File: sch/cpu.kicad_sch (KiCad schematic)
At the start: 10 parts

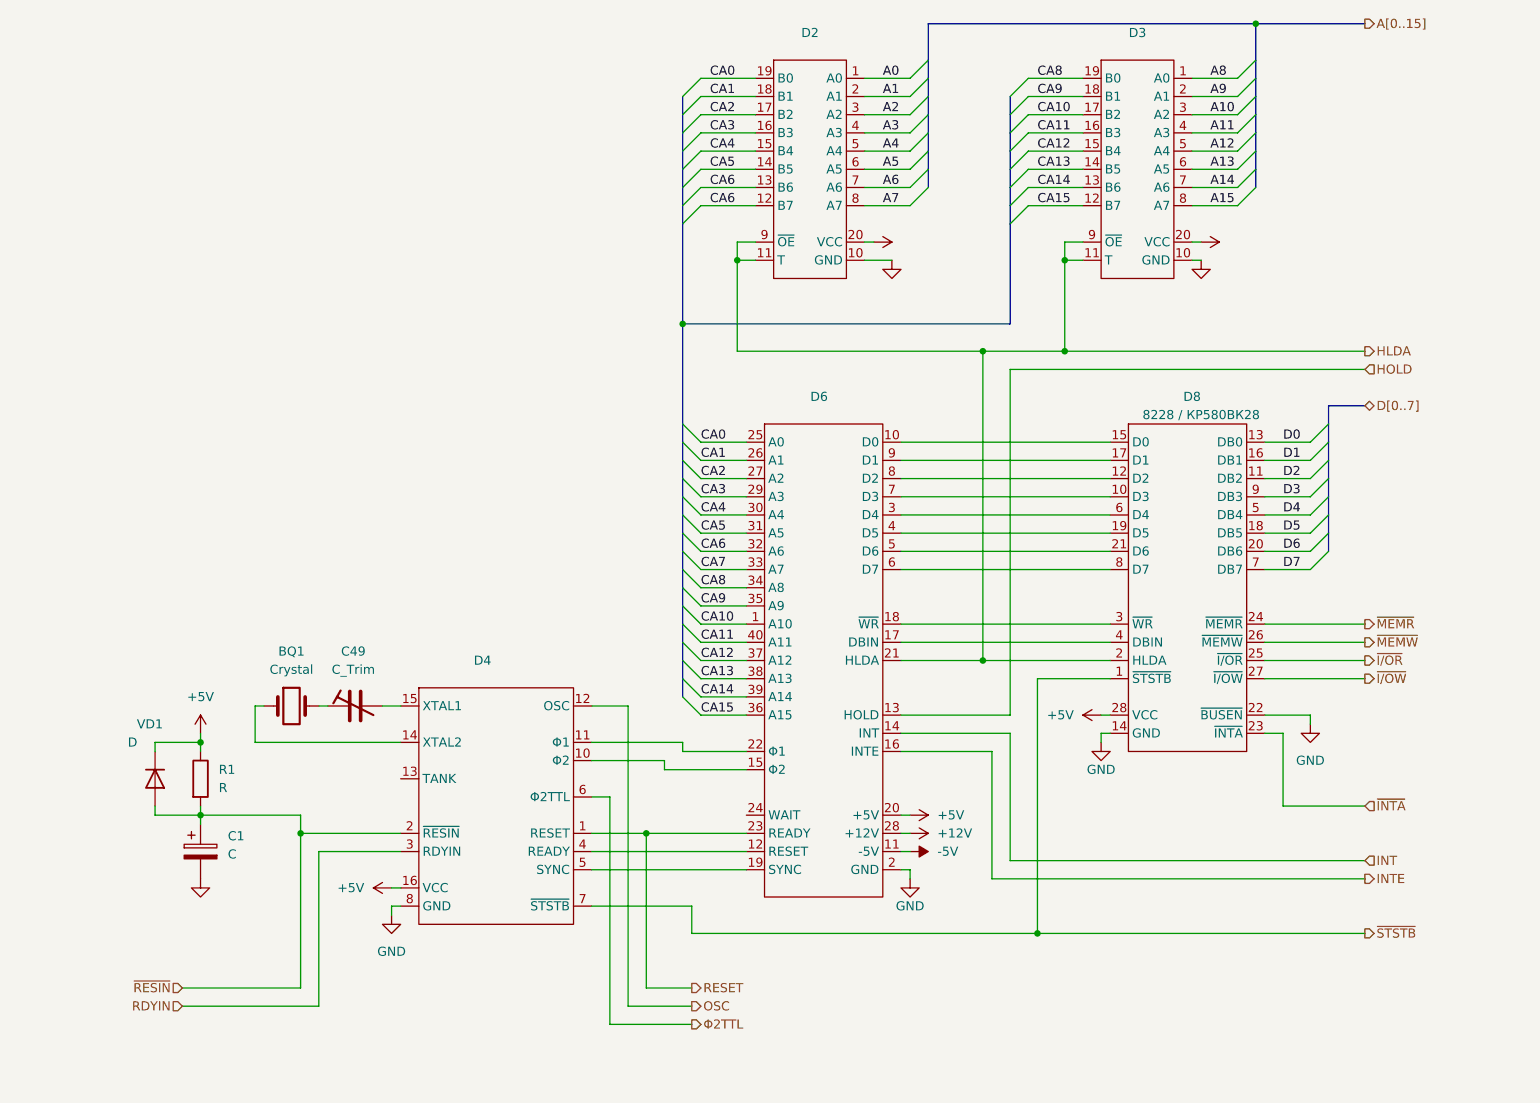
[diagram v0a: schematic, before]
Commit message: Schematic: ROM block
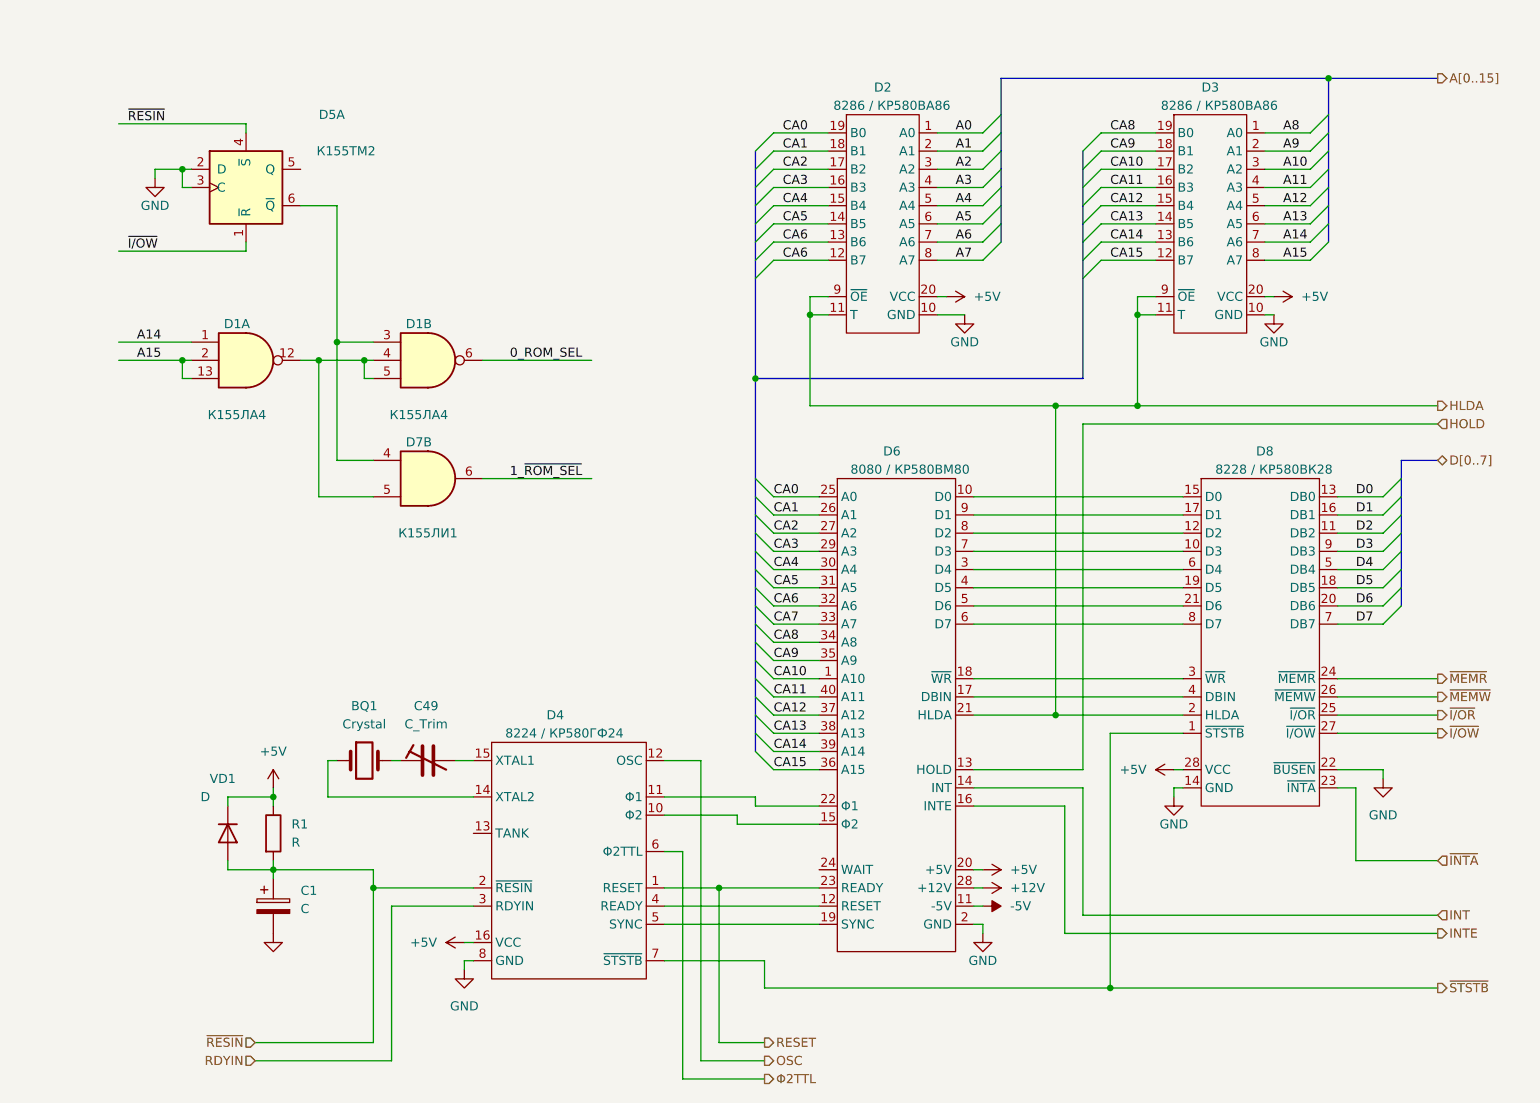
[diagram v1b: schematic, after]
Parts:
- added D1: (no value), symbol 74xx:74LS10
- added D5: (no value), symbol 74xx:74LS74
- added D7: (no value), symbol 74xx:74LS08
- D2, D3: value (none) -> 8286 / КР580ВА86
- D4: value (none) -> 8224 / КР580ГФ24
- D6: value (none) -> 8080 / КР580ВМ80
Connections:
- net A14: now also D1.1
- net A15: now also D1.13, D1.2
- net GND: now also D5.2 (D), D5.3 (C)
- net ~{I/OW}: now also D5.1 (~{R})
- net ~{RESIN}: now also D5.4 (~{S})
- new net: D1.3, D5.6 (~{Q}), D7.4
- new net: D1.12, D1.4, D1.5, D7.5
- new net 0_ROM_SEL: D1.6
- new net 1_~{ROM_SEL}: D7.6
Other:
- moved on the sheet: BQ1, C1, C49, D2, D3, D4, D6, D8, R1, VD1

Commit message: Added RAM block schematic placeholder
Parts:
- D1: value (none) -> 7410
- D5: value (none) -> 74LS74
- D7: value (none) -> 7408
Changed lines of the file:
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@@
     (in_bom yes) (on_board yes)
     (property "Reference" "D1" (id 0) (at 76.2 60.96 0))
-    (property "Value" "" (id 1) (at 76.2 71.12 0))
+    (property "Value" "7410" (id 1) (at 76.2 71.12 0))
     (property "Footprint" "" (id 2) (at 77.47 66.04 0)
       (effects (font (size 1.27 1.27)) hide)
@@
     (in_bom yes) (on_board yes)
     (property "Reference" "D1" (id 0) (at 50.8 60.96 0))
-    (property "Value" "" (id 1) (at 50.8 71.12 0))
+    (property "Value" "7410" (id 1) (at 50.8 71.12 0))
     (property "Footprint" "" (id 2) (at 52.07 66.04 0)
       (effects (font (size 1.27 1.27)) hide)
@@
       (effects (font (size 1.27 1.27)) (justify left))
     )
-    (property "Value" "" (id 1) (at 62.23 34.29 0)
+    (property "Value" "74LS74" (id 1) (at 62.23 34.29 0)
       (effects (font (size 1.27 1.27)) (justify left))
     )
@@
     (in_bom yes) (on_board yes)
     (property "Reference" "D7" (id 0) (at 76.2 77.47 0))
-    (property "Value" "" (id 1) (at 76.2 87.63 0))
+    (property "Value" "7408" (id 1) (at 76.2 87.63 0))
     (property "Footprint" "" (id 2) (at 77.47 82.55 0)
       (effects (font (size 1.27 1.27)) hide)

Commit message: Sch: CPU sheet - corrected address buffer pin assignment
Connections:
- net A10: now also D3.8 (A7); no longer D3.3 (A2)
- net A11: now also D3.7 (A6); no longer D3.4 (A3)
- net A12: now also D3.4 (A3); no longer D3.5 (A4)
- net A13: now also D3.5 (A4); no longer D3.6 (A5)
- net A14: now also D3.6 (A5); no longer D3.7 (A6)
- net A15: now also D3.3 (A2); no longer D3.8 (A7)
- net CA10: now also D3.12 (B7); no longer D3.17 (B2)
- net CA11: now also D3.13 (B6); no longer D3.16 (B3)
- net CA12: now also D3.16 (B3); no longer D3.15 (B4)
- net CA13: now also D3.15 (B4); no longer D3.14 (B5)
- net CA14: now also D3.14 (B5); no longer D3.13 (B6)
- net CA15: now also D3.17 (B2); no longer D3.12 (B7)
- net CA6: no longer D2.12 (B7)
- net CA7: now also D2.12 (B7)
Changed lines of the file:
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@@
     (stroke (width 0) (type default) (color 0 0 0 0))
   )
-  (label "A13" (at 196.85 46.99 0)
+  (label "A14" (at 196.85 46.99 0)
     (effects (font (size 1.27 1.27)) (justify left bottom))
   )
@@
     (effects (font (size 1.27 1.27)) (justify left bottom))
   )
-  (label "CA15" (at 172.72 52.07 0)
+  (label "CA10" (at 172.72 52.07 0)
     (effects (font (size 1.27 1.27)) (justify left bottom))
   )
@@
     (effects (font (size 1.27 1.27)) (justify left bottom))
   )
-  (label "CA11" (at 172.72 41.91 0)
+  (label "CA12" (at 172.72 41.91 0)
     (effects (font (size 1.27 1.27)) (justify left bottom))
   )
@@
     (effects (font (size 1.27 1.27)) (justify left bottom))
   )
-  (label "CA12" (at 172.72 44.45 0)
+  (label "CA13" (at 172.72 44.45 0)
     (effects (font (size 1.27 1.27)) (justify left bottom))
   )
-  (label "CA6" (at 127 52.07 0)
+  (label "CA7" (at 127 52.07 0)
     (effects (font (size 1.27 1.27)) (justify left bottom))
   )
@@
     (effects (font (size 1.27 1.27)) (justify left bottom))
   )
-  (label "CA13" (at 172.72 46.99 0)
+  (label "CA14" (at 172.72 46.99 0)
     (effects (font (size 1.27 1.27)) (justify left bottom))
   )
@@
     (effects (font (size 1.27 1.27)) (justify left bottom))
   )
-  (label "A12" (at 196.85 44.45 0)
+  (label "A13" (at 196.85 44.45 0)
     (effects (font (size 1.27 1.27)) (justify left bottom))
   )
@@
     (effects (font (size 1.27 1.27)) (justify left bottom))
   )
-  (label "CA10" (at 172.72 39.37 0)
+  (label "CA15" (at 172.72 39.37 0)
     (effects (font (size 1.27 1.27)) (justify left bottom))
   )
-  (label "A15" (at 196.85 52.07 0)
+  (label "A10" (at 196.85 52.07 0)
     (effects (font (size 1.27 1.27)) (justify left bottom))
   )
@@
     (effects (font (size 1.27 1.27)) (justify left bottom))
   )
-  (label "A11" (at 196.85 41.91 0)
+  (label "A12" (at 196.85 41.91 0)
     (effects (font (size 1.27 1.27)) (justify left bottom))
   )
@@
     (effects (font (size 1.27 1.27)) (justify left bottom))
   )
-  (label "CA14" (at 172.72 49.53 0)
+  (label "CA11" (at 172.72 49.53 0)
     (effects (font (size 1.27 1.27)) (justify left bottom))
   )
@@
     (effects (font (size 1.27 1.27)) (justify left bottom))
   )
-  (label "A10" (at 196.85 39.37 0)
+  (label "A15" (at 196.85 39.37 0)
     (effects (font (size 1.27 1.27)) (justify left bottom))
   )
@@
     (effects (font (size 1.27 1.27)) (justify left bottom))
   )
-  (label "A14" (at 196.85 49.53 0)
+  (label "A11" (at 196.85 49.53 0)
     (effects (font (size 1.27 1.27)) (justify left bottom))
   )

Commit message: Minor renames
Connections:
- net ~{REMAP}: now reaches D1.3, D5.6 (~{Q}), D7.4
- net 0_ROM_SEL renamed ROM_OE
- net 1_~{ROM_SEL} renamed ~{ROM_OE}
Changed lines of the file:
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@@
   (junction (at 118.11 139.7) (diameter 0) (color 0 0 0 0)
   )
-  (junction (at 64.77 63.5) (diameter 0) (color 0 0 0 0)
-  )
   (junction (at 123.19 68.58) (diameter 0) (color 0 0 0 0)
   )
   (junction (at 62.23 66.04) (diameter 0) (color 0 0 0 0)
   )
+  (junction (at 68.58 63.5) (diameter 0) (color 0 0 0 0)
+  )
   (junction (at 203.2 26.67) (diameter 0) (color 0 0 0 0)
   )
@@
     (stroke (width 0) (type default) (color 0 0 0 0))
   )
+  (wire (pts (xy 68.58 63.5) (xy 69.85 63.5))
+    (stroke (width 0) (type default) (color 0 0 0 0))
+  )
   (bus (pts (xy 123.19 113.03) (xy 123.19 115.57))
     (stroke (width 0) (type default) (color 0 0 0 0))
@@
     (stroke (width 0) (type default) (color 0 0 0 0))
   )
+  (wire (pts (xy 68.58 63.5) (xy 64.77 63.5))
+    (stroke (width 0) (type default) (color 0 0 0 0))
+  )
   (wire (pts (xy 110.49 142.24) (xy 132.08 142.24))
     (stroke (width 0) (type default) (color 0 0 0 0))
@@
     (stroke (width 0) (type default) (color 0 0 0 0))
   )
-  (wire (pts (xy 64.77 63.5) (xy 69.85 63.5))
-    (stroke (width 0) (type default) (color 0 0 0 0))
-  )
   (wire (pts (xy 153.67 139.7) (xy 154.94 139.7))
     (stroke (width 0) (type default) (color 0 0 0 0))
@@
     (stroke (width 0) (type default) (color 0 0 0 0))
   )
-  (wire (pts (xy 59.69 44.45) (xy 64.77 44.45))
+  (wire (pts (xy 59.69 44.45) (xy 68.58 44.45))
     (stroke (width 0) (type default) (color 0 0 0 0))
   )
@@
     (stroke (width 0) (type default) (color 0 0 0 0))
   )
-  (wire (pts (xy 64.77 44.45) (xy 64.77 63.5))
+  (wire (pts (xy 68.58 44.45) (xy 68.58 63.5))
     (stroke (width 0) (type default) (color 0 0 0 0))
   )
@@
     (effects (font (size 1.27 1.27)) (justify left bottom))
   )
-  (label "1_~{ROM_SEL}" (at 88.9 82.55 0)
+  (label "~{ROM_OE}" (at 88.9 82.55 0)
     (effects (font (size 1.27 1.27)) (justify left bottom))
   )
@@
     (effects (font (size 1.27 1.27)) (justify left bottom))
   )
-  (label "0_ROM_SEL" (at 88.9 66.04 0)
-    (effects (font (size 1.27 1.27)) (justify left bottom))
-  )
+  (label "~{REMAP}" (at 60.96 44.45 0)
+    (effects (font (size 1.27 1.27)) (justify left bottom))
+  )
+  (label "ROM_OE" (at 88.9 66.04 0)
+    (effects (font (size 1.27 1.27)) (justify left bottom))
+  )

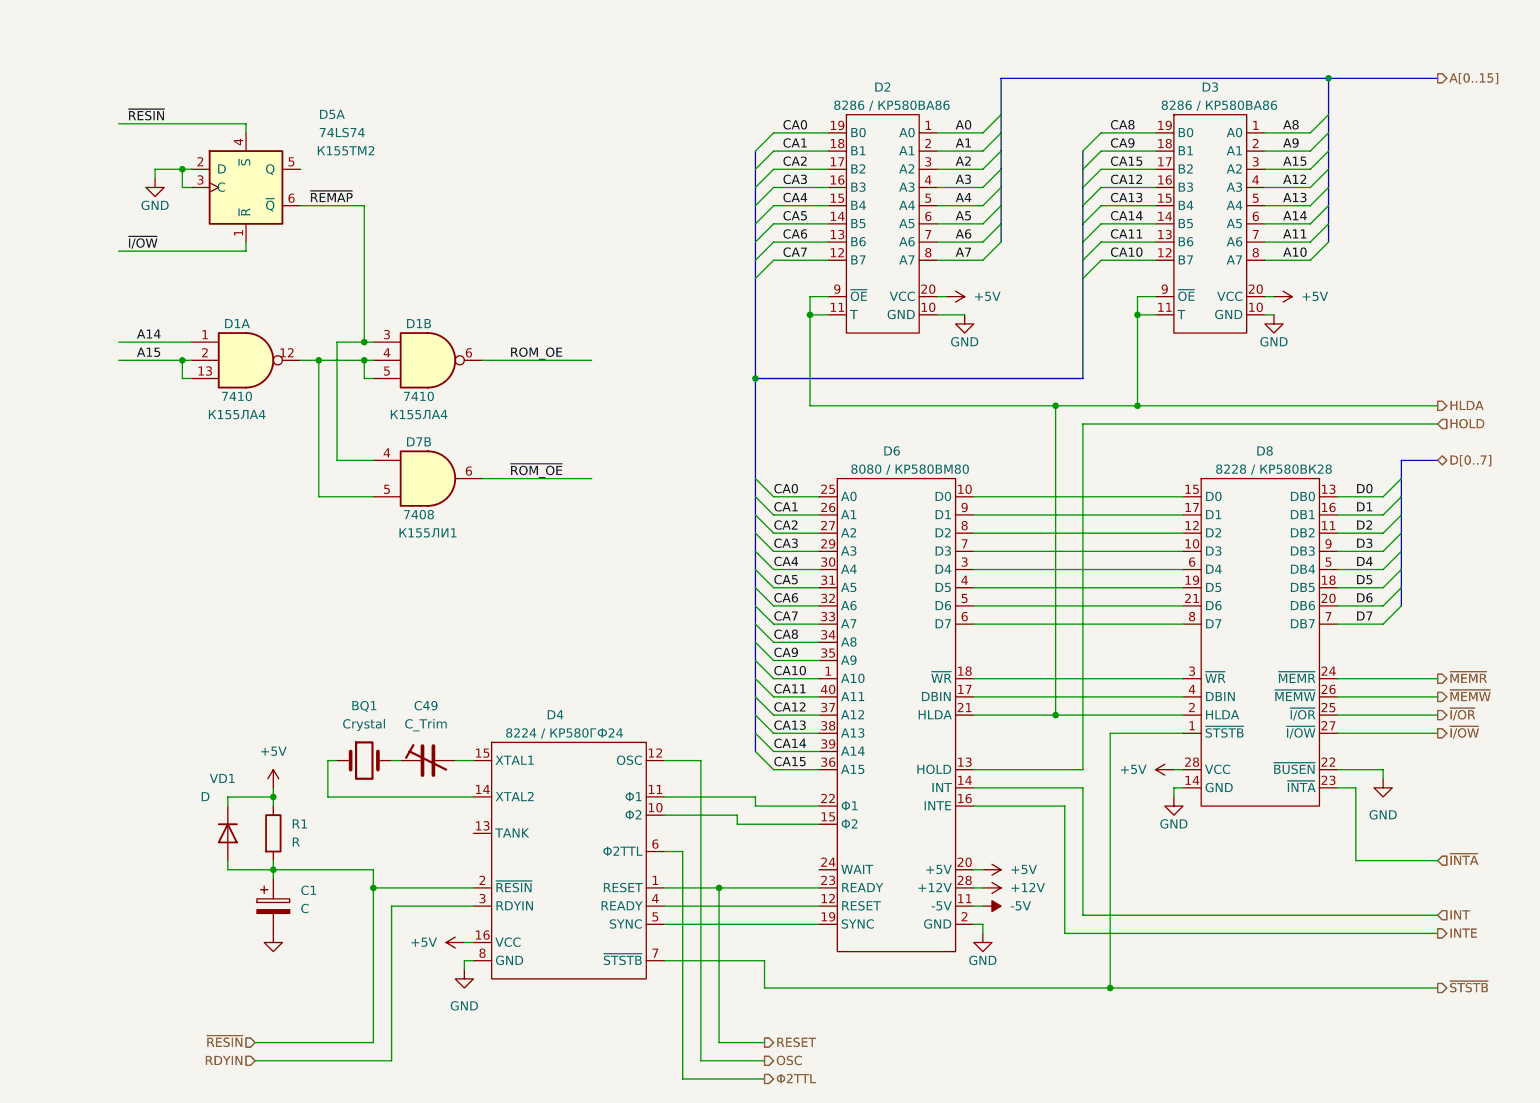
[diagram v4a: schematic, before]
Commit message: Sch: mem remapping circuit moved to ROM sheet
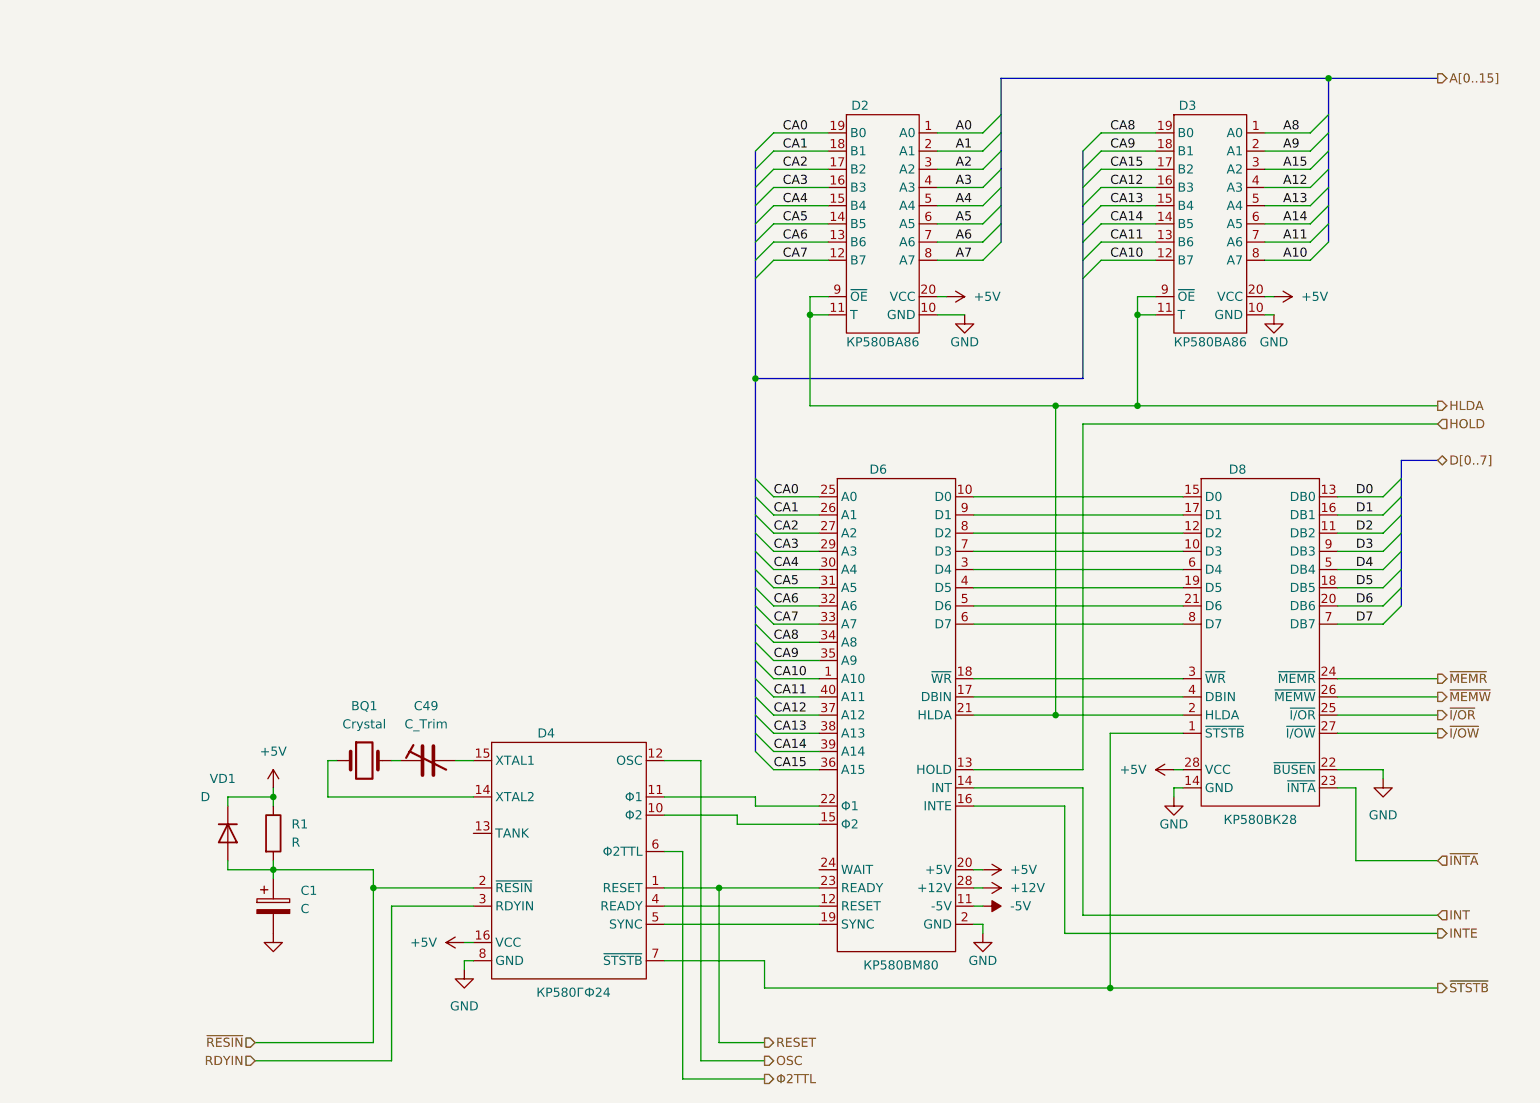
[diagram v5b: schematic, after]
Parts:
- removed D1: 7410, symbol 74xx:74LS10
- removed D5: 74LS74, symbol 74xx:74LS74
- removed D7: 7408, symbol 74xx:74LS08
- D2, D3: value 8286 / КР580ВА86 -> (none); CCCP (none) -> КР580ВА86
- D4: value 8224 / КР580ГФ24 -> (none); CCCP (none) -> КР580ГФ24
- D6: value 8080 / КР580ВМ80 -> (none); CCCP (none) -> КР580ВМ80
- D8: value 8228 / КР580ВК28 -> (none); CCCP (none) -> КР580ВК28
